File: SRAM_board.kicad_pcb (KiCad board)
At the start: 4 copper layers, 108 x 70 mm, 90 parts, among them J1 JP3, J10 Optional Interrupt Pins, J11 Optional Interrupt Pin, J12 GPIO 1, J13 GPIO 0, J14 USB_OTG, J2 JP6, J3 JP2, J4 JP5, J5 Screw_Terminal_01x09, J6 Screw_Terminal_01x06, J7 Optional I2C/UART, J9 Optional Interrupt Pin, SW1 KEY1, SW2 KEY0, U1 LD1085D2T33R, U2 MS561101BA03-50, U3 IIS2MDCTR, U4 GS832032AGT-150I, U5 BMI055, U6 ICM-20689, U7 FT232RL, U8 CDCLVC1102

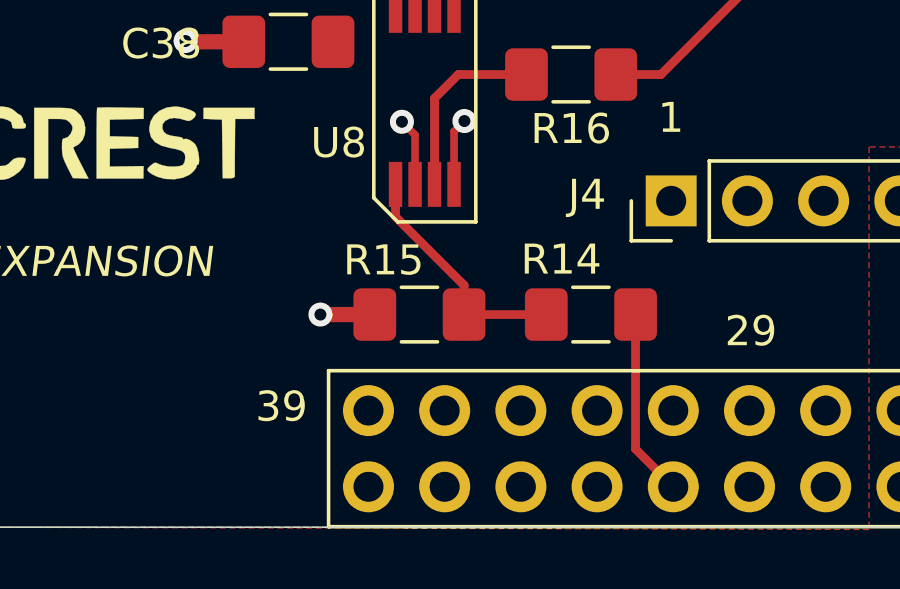
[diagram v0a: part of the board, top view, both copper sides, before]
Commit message: switch sram clock pin
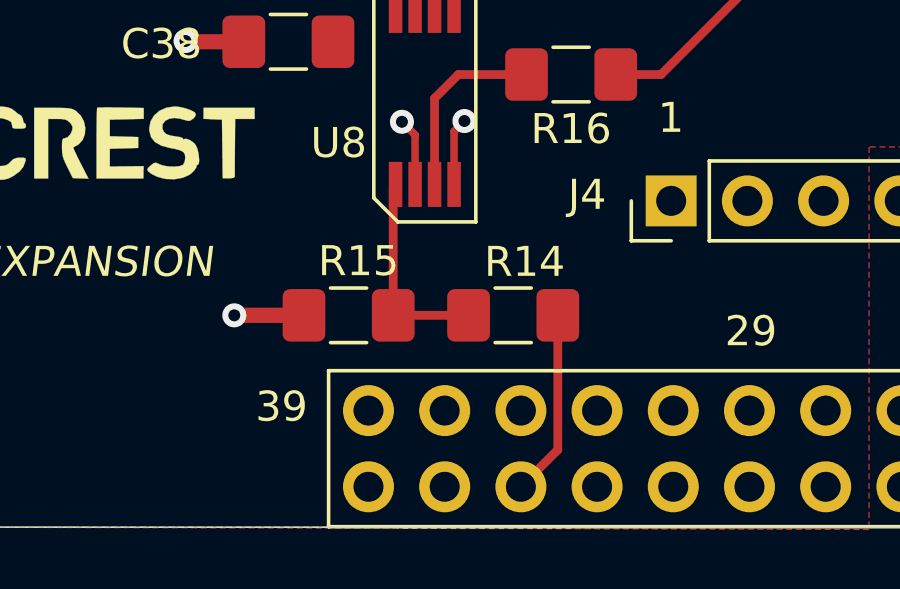
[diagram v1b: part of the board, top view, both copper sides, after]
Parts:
- moved R14 2.59 mm to (25.3, -3.17)
- moved R15 2.36 mm to (19.8, -3.17)
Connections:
- J13 pad 32: /CLK_IN -> /~ADSP
- J13 pad 34: /~ADSP -> /~BW
- J13 pad 36: /~BW -> /CLK_IN
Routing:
- net /~ADSP: track 36.5 -> 38.6 mm
- net /~BW: track 42.1 -> 44.2 mm
- net Net-(R14-Pad1): track 8.03 -> 6.91 mm
- net GND: track 209.0 -> 209.5 mm
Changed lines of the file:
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@@
   )
   (setup
-    (last_trace_width 0.25)
+    (last_trace_width 0.0889)
     (user_trace_width 0.0889)
     (user_trace_width 0.1524)
@@
       (net 148 /~E3))
     (pad 32 thru_hole oval (at 2.54 38.1 270) (size 1.7 1.7) (drill 1) (layers *.Cu *.Mask)
-      (net 160 /CLK_IN))
+      (net 142 /~ADSP))
     (pad 33 thru_hole oval (at 0 40.64 270) (size 1.7 1.7) (drill 1) (layers *.Cu *.Mask)
       (net 144 /~G))
     (pad 34 thru_hole oval (at 2.54 40.64 270) (size 1.7 1.7) (drill 1) (layers *.Cu *.Mask)
-      (net 142 /~ADSP))
+      (net 145 /~BW))
     (pad 35 thru_hole oval (at 0 43.18 270) (size 1.7 1.7) (drill 1) (layers *.Cu *.Mask)
       (net 141 /~ADV))
     (pad 36 thru_hole oval (at 2.54 43.18 270) (size 1.7 1.7) (drill 1) (layers *.Cu *.Mask)
-      (net 145 /~BW))
+      (net 160 /CLK_IN))
     (pad 37 thru_hole oval (at 0 45.72 270) (size 1.7 1.7) (drill 1) (layers *.Cu *.Mask)
       (net 146 /~GW))
@@
   )
   (module Resistor_SMD:R_1206_3216Metric_Pad1.42x1.75mm_HandSolder (layer F.Cu)
-    (at 27.9146 -3.2004)
+    (at 25.3238 -3.175)
     (descr "Resistor SMD 1206 (3216 Metric), square (rectangular) end terminal, IPC_7351 nominal with elongated pad for handsoldering. (Body size source: http://www.tortai-tech.com/upload/download/2011102023233369053.pdf), generated with kicad-footprint-generator")
     (tags "resistor handsolder")
     (attr smd)
-    (fp_text reference R14 (at -0.9906 -1.8288) (layer F.SilkS)
+    (fp_text reference R14 (at 0.381 -1.778) (layer F.SilkS)
       (effects (font (size 1 1) (thickness 0.15)))
     )
@@
   )
   (module Resistor_SMD:R_1206_3216Metric_Pad1.42x1.75mm_HandSolder (layer F.Cu)
-    (at 22.1996 -3.2004)
+    (at 19.8374 -3.175)
     (descr "Resistor SMD 1206 (3216 Metric), square (rectangular) end terminal, IPC_7351 nominal with elongated pad for handsoldering. (Body size source: http://www.tortai-tech.com/upload/download/2011102023233369053.pdf), generated with kicad-footprint-generator")
     (tags "resistor handsolder")
     (attr smd)
-    (fp_text reference R15 (at -1.1938 -1.8034) (layer F.SilkS)
+    (fp_text reference R15 (at 0.3302 -1.8034) (layer F.SilkS)
       (effects (font (size 1 1) (thickness 0.15)))
     )
@@
   (segment (start 14.4272 -12.2936) (end 14.4018 -12.319) (width 0.508) (layer F.Cu) (net 2))
   (segment (start 16.3433 -12.2936) (end 14.4272 -12.2936) (width 0.508) (layer F.Cu) (net 2) (status 10))
-  (via (at 18.8976 -3.2004) (size 0.8) (drill 0.4) (layers F.Cu B.Cu) (net 2))
-  (segment (start 20.7121 -3.2004) (end 18.8976 -3.2004) (width 0.508) (layer F.Cu) (net 2) (status 10))
+  (via (at 16.0274 -3.175) (size 0.8) (drill 0.4) (layers F.Cu B.Cu) (net 2))
+  (segment (start 18.3499 -3.175) (end 16.0274 -3.175) (width 0.508) (layer F.Cu) (net 2))
   (segment (start 82.7638 -52.2261) (end 82.7786 -52.2113) (width 0.1524) (layer F.Cu) (net 4) (status 30))
   (segment (start 82.7638 -54.6066) (end 82.7638 -52.2261) (width 0.1524) (layer F.Cu) (net 4) (status 30))
@@
   (via (at 40.279276 -22.199731) (size 0.6) (drill 0.2) (layers F.Cu B.Cu) (net 142))
   (segment (start 40.6568 -20.03572) (end 40.6568 -21.822207) (width 0.0889) (layer F.Cu) (net 142) (status 10))
-  (segment (start 40.279276 -22.199731) (end 40.279276 -20.583927) (width 0.0889) (layer In2.Cu) (net 142))
-  (segment (start 37.969579 -19.835687) (end 37.091678 -18.957786) (width 0.0889) (layer In2.Cu) (net 142))
   (segment (start 39.531036 -19.835687) (end 37.969579 -19.835687) (width 0.0889) (layer In2.Cu) (net 142))
-  (segment (start 40.279276 -20.583927) (end 39.531036 -19.835687) (width 0.0889) (layer In2.Cu) (net 142))
-  (segment (start 37.091678 -18.957786) (end 36.068 -18.957786) (width 0.0889) (layer In2.Cu) (net 142))
-  (segment (start 33.568565 -18.957785) (end 26.45741 -11.84663) (width 0.0889) (layer In2.Cu) (net 142))
-  (segment (start 36.068 -18.957786) (end 33.568565 -18.957785) (width 0.0889) (layer In2.Cu) (net 142))
+  (segment (start 37.969579 -19.835687) (end 37.091678 -18.957786) (width 0.0889) (layer In2.Cu) (net 142))
+  (segment (start 27.4828 1.27) (end 29.39 1.27) (width 0.0889) (layer In2.Cu) (net 142))
   (segment (start 26.45741 -11.84663) (end 26.45741 -2.14961) (width 0.0889) (layer In2.Cu) (net 142))
-  (segment (start 27.025549 1.445549) (end 28.12 2.54) (width 0.0889) (layer In2.Cu) (net 142) (status 20))
-  (segment (start 27.025549 -1.581471) (end 27.025549 1.445549) (width 0.0889) (layer In2.Cu) (net 142))
+  (segment (start 40.279276 -22.199731) (end 40.279276 -20.583927) (width 0.0889) (layer In2.Cu) (net 142))
+  (segment (start 29.39 1.27) (end 30.66 2.54) (width 0.0889) (layer In2.Cu) (net 142))
+  (segment (start 33.568565 -18.957785) (end 26.45741 -11.84663) (width 0.0889) (layer In2.Cu) (net 142))
+  (segment (start 37.091678 -18.957786) (end 33.568565 -18.957785) (width 0.0889) (layer In2.Cu) (net 142))
   (segment (start 26.45741 -2.14961) (end 27.025549 -1.581471) (width 0.0889) (layer In2.Cu) (net 142))
+  (segment (start 40.279276 -20.583927) (end 39.531036 -19.835687) (width 0.0889) (layer In2.Cu) (net 142))
+  (segment (start 27.025549 -1.581471) (end 27.025549 0.812749) (width 0.0889) (layer In2.Cu) (net 142))
+  (segment (start 27.025549 0.812749) (end 27.4828 1.27) (width 0.0889) (layer In2.Cu) (net 142))
   (segment (start 41.3068 -20.03572) (end 41.3068 -32.6708) (width 0.0889) (layer F.Cu) (net 143) (status 10))
   (segment (start 48.456799 -49.053801) (end 48.4124 -49.0982) (width 0.0889) (layer In2.Cu) (net 143))
@@
   (segment (start 42.6068 -22.277879) (end 42.0116 -22.873079) (width 0.0889) (layer F.Cu) (net 145))
   (segment (start 42.6068 -20.03572) (end 42.6068 -22.277879) (width 0.0889) (layer F.Cu) (net 145) (status 10))
-  (segment (start 38.448263 -23.760051) (end 37.9476 -23.259388) (width 0.0889) (layer In2.Cu) (net 145))
-  (segment (start 41.467149 -23.760051) (end 38.448263 -23.760051) (width 0.0889) (layer In2.Cu) (net 145))
+  (segment (start 37.9476 -23.259388) (end 37.9476 -20.630868) (width 0.0889) (layer In2.Cu) (net 145))
+  (segment (start 24.3332 0.762) (end 24.8412 1.27) (width 0.0889) (layer In2.Cu) (net 145))
   (segment (start 42.0116 -23.2156) (end 41.467149 -23.760051) (width 0.0889) (layer In2.Cu) (net 145))
   (segment (start 37.9476 -20.630868) (end 36.852338 -19.535606) (width 0.0889) (layer In2.Cu) (net 145))
-  (segment (start 37.9476 -23.259388) (end 37.9476 -20.630868) (width 0.0889) (layer In2.Cu) (net 145))
-  (segment (start 33.329226 -19.535606) (end 25.87959 -12.08597) (width 0.0889) (layer In2.Cu) (net 145))
+  (segment (start 41.467149 -23.760051) (end 38.448263 -23.760051) (width 0.0889) (layer In2.Cu) (net 145))
   (segment (start 36.852338 -19.535606) (end 33.329226 -19.535606) (width 0.0889) (layer In2.Cu) (net 145))
-  (segment (start 25.87959 -12.08597) (end 25.87959 -2.84397) (width 0.0889) (layer In2.Cu) (net 145))
+  (segment (start 38.448263 -23.760051) (end 37.9476 -23.259388) (width 0.0889) (layer In2.Cu) (net 145))
+  (segment (start 33.329226 -19.535606) (end 25.87959 -12.08597) (width 0.0889) (layer In2.Cu) (net 145))
+  (segment (start 26.85 1.27) (end 28.12 2.54) (width 0.0889) (layer In2.Cu) (net 145))
   (segment (start 25.87959 -2.84397) (end 24.3332 -1.29758) (width 0.0889) (layer In2.Cu) (net 145))
-  (segment (start 24.3332 1.2932) (end 25.58 2.54) (width 0.0889) (layer In2.Cu) (net 145) (status 20))
-  (segment (start 24.3332 1.0414) (end 24.3332 1.2932) (width 0.0889) (layer In2.Cu) (net 145))
-  (segment (start 24.3332 -1.29758) (end 24.3332 1.0414) (width 0.0889) (layer In2.Cu) (net 145))
-  (segment (start 24.3332 1.0414) (end 24.3332 1.2446) (width 0.0889) (layer In2.Cu) (net 145))
+  (segment (start 24.3332 -1.29758) (end 24.3332 0.762) (width 0.0889) (layer In2.Cu) (net 145))
+  (segment (start 24.8412 1.27) (end 26.85 1.27) (width 0.0889) (layer In2.Cu) (net 145))
+  (segment (start 25.87959 -12.08597) (end 25.87959 -2.84397) (width 0.0889) (layer In2.Cu) (net 145))
   (via (at 42.0116 -24.015603) (size 0.6) (drill 0.2) (layers F.Cu B.Cu) (net 146))
   (segment (start 42.017385 -24.015603) (end 42.0116 -24.015603) (width 0.0889) (layer F.Cu) (net 146))
@@
   (segment (start 14.645499 -34.817) (end 15.958 -34.817) (width 0.2) (layer F.Cu) (net 158) (status 20))
   (segment (start 23.2024 -34.7726) (end 23.158 -34.817) (width 0.1524) (layer F.Cu) (net 159) (status 30))
-  (segment (start 29.4021 1.2821) (end 30.66 2.54) (width 0.29337) (layer F.Cu) (net 160) (status 20))
-  (segment (start 29.4021 -3.2004) (end 29.4021 1.2821) (width 0.29337) (layer F.Cu) (net 160) (status 10))
-  (segment (start 26.4271 -3.2004) (end 23.6871 -3.2004) (width 0.29337) (layer F.Cu) (net 161) (status 30))
-  (segment (start 21.4024 -6.4601) (end 21.4024 -7.5394) (width 0.29337) (layer F.Cu) (net 161) (status 20))
-  (segment (start 23.6871 -4.1754) (end 21.4024 -6.4601) (width 0.29337) (layer F.Cu) (net 161))
-  (segment (start 23.6871 -3.2004) (end 23.6871 -4.1754) (width 0.29337) (layer F.Cu) (net 161) (status 10))
+  (segment (start 26.8113 1.3087) (end 26.8113 -3.175) (width 0.29337) (layer F.Cu) (net 160))
+  (segment (start 25.58 2.54) (end 26.8113 1.3087) (width 0.29337) (layer F.Cu) (net 160))
+  (segment (start 23.8363 -3.175) (end 21.3249 -3.175) (width 0.29337) (layer F.Cu) (net 161))
+  (segment (start 21.3249 -7.4619) (end 21.4024 -7.5394) (width 0.29337) (layer F.Cu) (net 161))
+  (segment (start 21.3249 -3.175) (end 21.3249 -7.4619) (width 0.29337) (layer F.Cu) (net 161))
   (segment (start 22.7024 -7.5394) (end 22.7024 -10.4088) (width 0.29337) (layer F.Cu) (net 162) (status 10))
   (segment (start 23.495 -11.2014) (end 25.7667 -11.2014) (width 0.29337) (layer F.Cu) (net 162) (status 20))
